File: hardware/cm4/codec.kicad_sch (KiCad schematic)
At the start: 14 parts, among them U2 WM8731SEDS, U4 AP2112K-3.3, Y1 12.288MHz

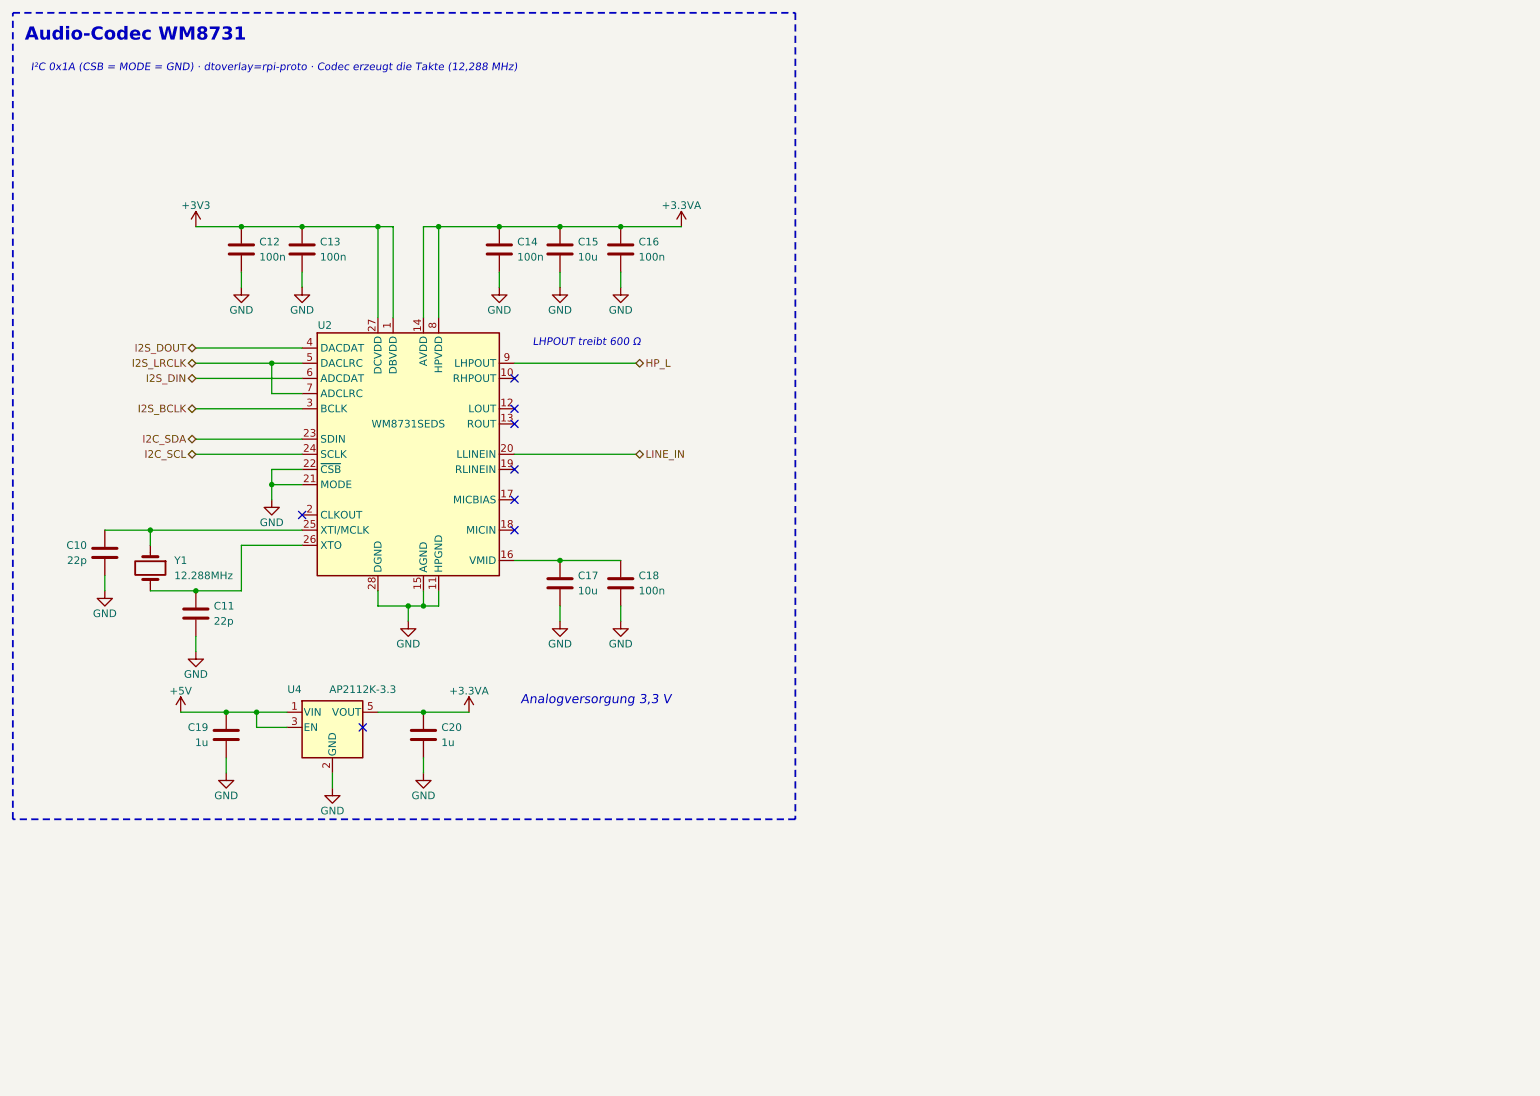
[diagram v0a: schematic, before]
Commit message: CM4-Schaltplan: Einzelblock-Blätter ohne Rahmen, Inhalt zentriert
kicadgen: Steht nur ein Block auf einem Blatt, entfällt der Rahmen (sein Titel wird
Blatttitel) und der Inhalt wird auf dem Blatt zentriert (über dem Schriftfeld, auf dem
1,27-mm-Raster). Hinweistexte der CM4-Blätter an die Schaltungen gerückt.

Co-Authored-By: Claude Opus 5.5 <noreply@anthropic.com>
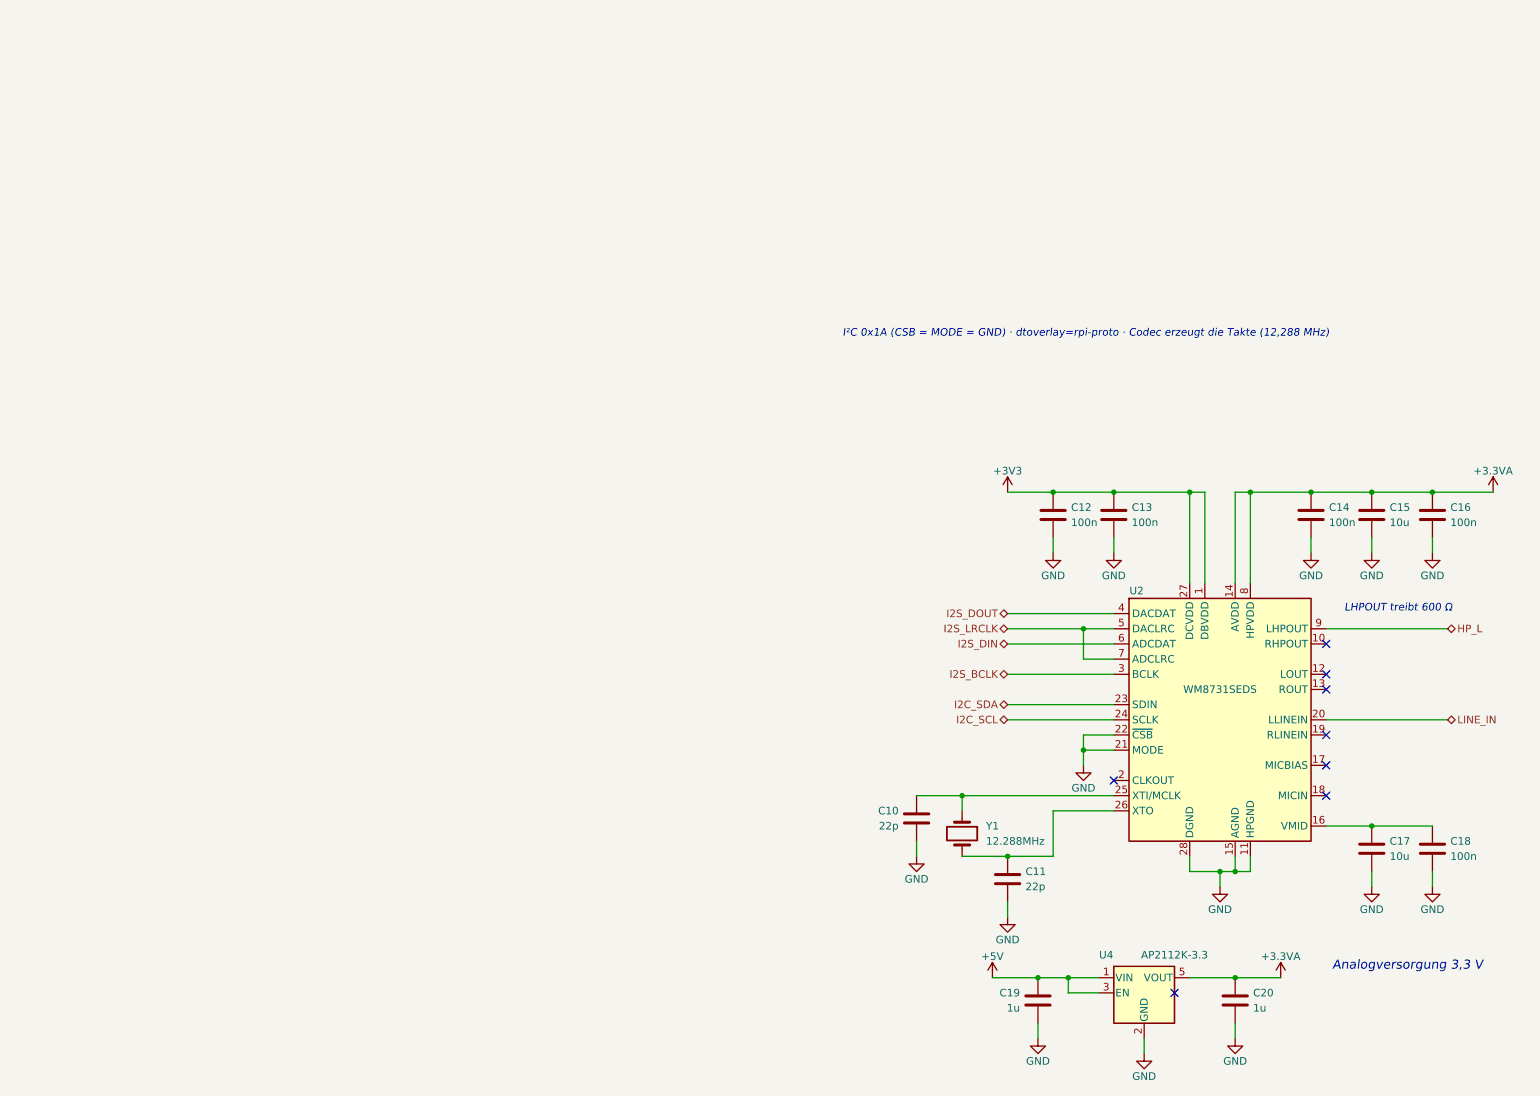
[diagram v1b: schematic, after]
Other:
- note removed: "Audio-Codec WM8731"
- title: Audio-Codec -> Audio-Codec WM8731
